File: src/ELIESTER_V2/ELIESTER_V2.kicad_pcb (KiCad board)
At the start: 4 copper layers, 102 x 86.2 mm, 309 parts, among them J1 Barrel_Jack_Switch, J10 Conn_01x04, J11 SIM_Card, J2 SCREEN CONN FPC 10PIN 1MM, J3 Conn_01x04, J4 Conn_01x04, J5 USB_B_Micro, J6 Conn_01x04, J7 Conn_01x04, J8 RJ45_Bel_SI-60062-F, J9 Conn_01x04, Q1 MMBT3904, Q11 MMBT3904, Q12 MMBT3904, Q2 MMBT3904, Q3 DMP3056L-7, Q4 DMP3056L-7, Q5 SI2302-HXY, Q6 DMP3056L-7, Q7 BSN20, Q8 BSN20, SW1 SW_Push, SW2 SW_Push, SW3 SW_Push, U1 WAS3157B, U10 PC817, U11 PC817, U12 W5500, U13 TBU-CA065-200-WH, U14 TPS56339DDC, U15 MAX485E, U16 TBU-CA065-200-WH, U17 SN74AHC1G125, U18 PC817, U19 ADS1115IDGS, U2 MAX3232, U20 PC817, U21 PC817, U22 PC817, U23 PC817, U24 PCF8574A, U25 SY8089AAAC, U26 SIM7000G, U3 ESP32 Wroom, U4 CH340T(SSOP20W), U5 WAS3157B, U6 PC817, U7 PC817, U8 TPS54331, U9 DS3231MZ_V__NRND, Y1 12MHz, Y2 25MHz

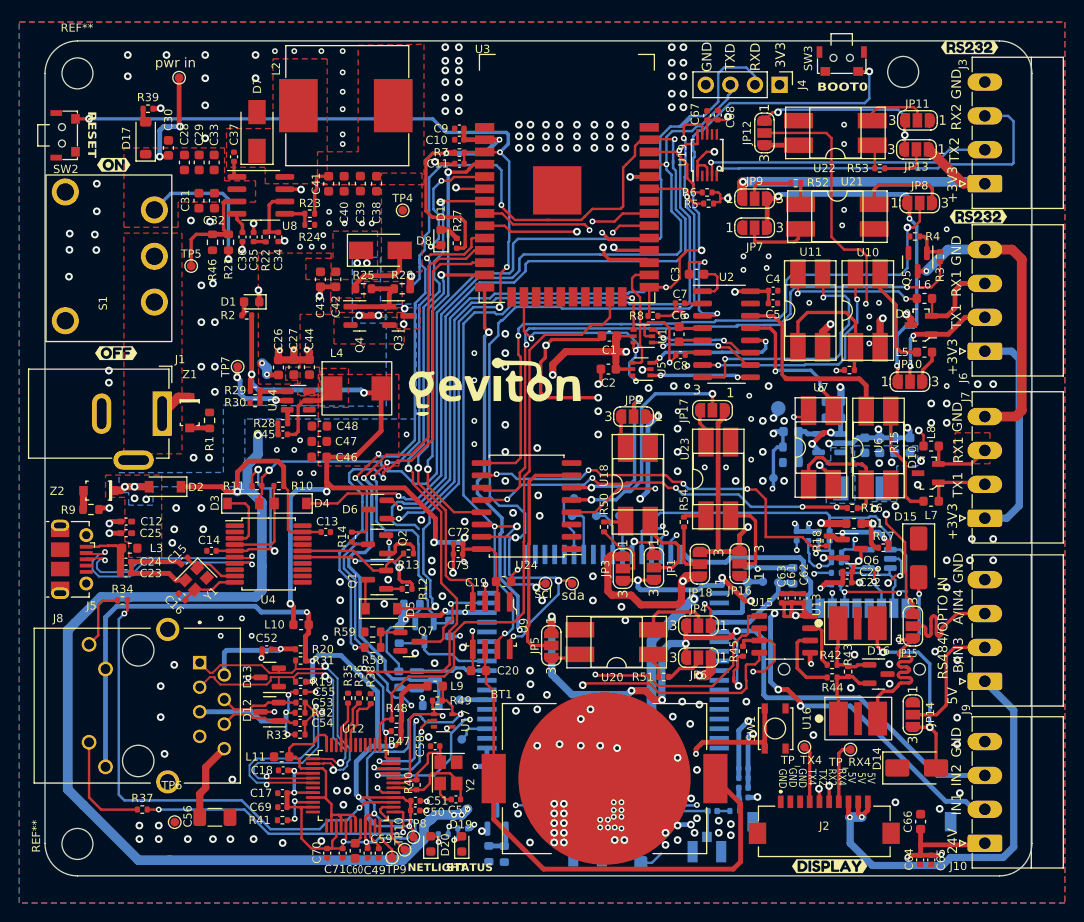
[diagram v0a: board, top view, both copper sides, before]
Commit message: update on antenna an LAN side
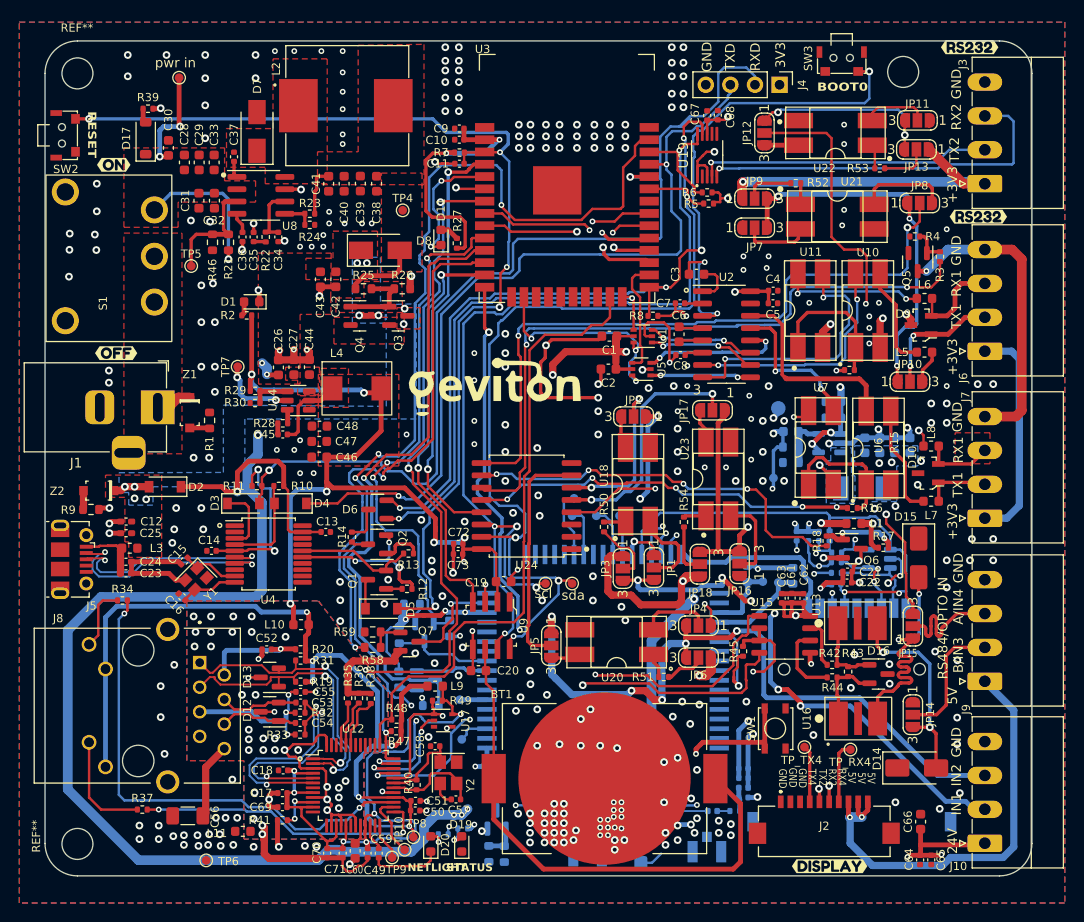
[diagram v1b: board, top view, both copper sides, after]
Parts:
- J1: footprint Connector_BarrelJack:BarrelJack_GCT_DCJ200-10-A_Horizontal -> Connector_BarrelJack:BarrelJack_Horizontal
- U19: footprint Package_SO:TSSOP-10_3x3mm_P0.5mm -> Package_SO:VSSOP-10_3x3mm_P0.5mm
- moved L11 8.68 mm to (181.1, 136.6)
- moved TP6 5.12 mm to (177.3, 139.6)
- moved C56 2.80 mm to (175.4, 135.0), turned to 180 degrees
- moved J1 0.79 mm to (172.3, 92.8), turned to 0 degrees
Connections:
- C17 pad 2: GND -> GNDA
- C18 pad 2: GND -> GNDA
- C49 pad 2: GND -> GNDA
- C52 pad 1: GND -> GNDA
- C55 pad 1: GND -> GNDA
- C69 pad 2: GND -> GNDA
- C70 pad 2: GND -> GNDA
- C71 pad 2: GND -> GNDA
- D12 pad 3: GND -> GNDA
- D13 pad 3: GND -> GNDA
- L11 pad 1: Net-(L11-Pad1) -> GNDA
- U12 pad 14: Net-(L11-Pad1) -> GNDA
- U12 pad 16: Net-(L11-Pad1) -> GNDA
- U12 pad 19: Net-(L11-Pad1) -> GNDA
- U12 pad 3: Net-(L11-Pad1) -> GNDA
- U12 pad 48: Net-(L11-Pad1) -> GNDA
- U12 pad 9: Net-(L11-Pad1) -> GNDA
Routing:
- net /ESP32_MCU/spi_MOSI: track 186.0 -> 110.7 mm, vias 7 -> 6
- net GNDA: track 0.00 -> 49.7 mm, vias 0 -> 38
- net GND: track 177.4 -> 206.7 mm, vias 336 -> 348
- net Net-(L11-Pad1): track 23.1 -> 0.00 mm
- net /SPI_ETH_INTERFACE_W5500/3V3A: track 69.0 -> 67.4 mm
- net /MAX485/IN4: track 50.6 -> 49.9 mm
- net /ESP32_MCU/soft_uart_tx: track 54.8 -> 54.3 mm
- added copper zone on B.Cu, net GNDA
- added copper zone on F.Cu, net GNDA
- added copper zone on In1.Cu, net GNDA
- added copper zone on In2.Cu, net GNDA
